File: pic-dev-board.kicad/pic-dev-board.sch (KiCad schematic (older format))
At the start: 44 parts, among them J1 Conn_GP0, J13 Conn_5V_GND, J15 Barrel_Jack_Switch, J16 RUN/~PGM, J17 I2C, J18 GP1(RA1)/RB6, J19 GP2(RA2)/RB4, J2 Conn_GP4, J20 Conn_TRISA, J3 Conn_GP1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

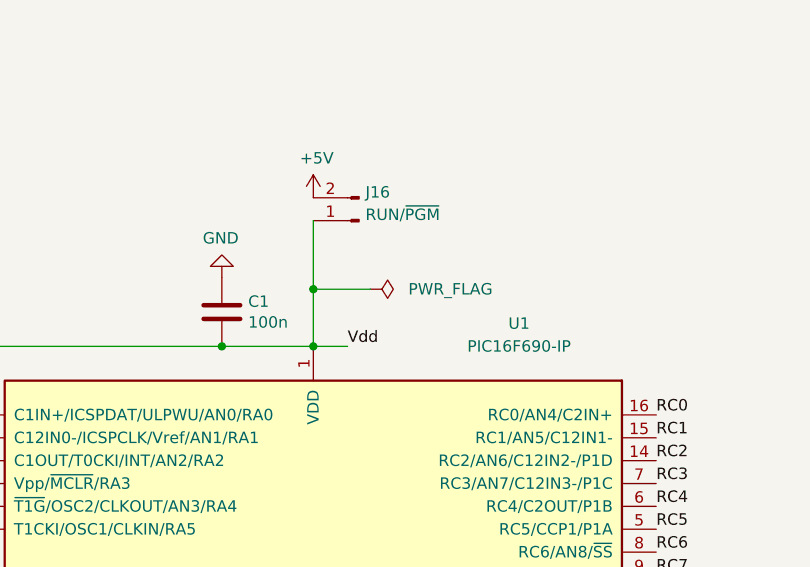
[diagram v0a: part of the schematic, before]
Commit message: removed unnecessary power-flag
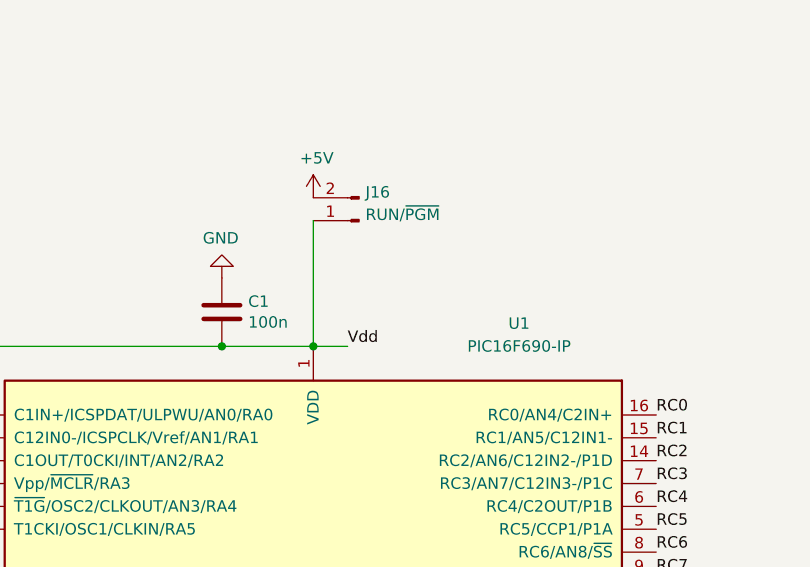
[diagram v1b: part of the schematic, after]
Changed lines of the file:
@@
 Sheet 1 2
 Title "PIC Development Board"
-Date "2020-08-24"
+Date "2020-08-26"
 Rev "2"
 Comp "Bernhard Bablok"
@@
 	-1   0    0    1
 $EndComp
-Wire Wire Line
-	5200 3500 5200 3800
-$Comp
-L power:PWR_FLAG #FLG0104
-U 1 1 5F37108D
-P 5450 3800
-F 0 "#FLG0104" H 5450 3875 50  0001 C CNN
-F 1 "PWR_FLAG" V 5450 4150 50  0000 C CNN
-F 2 "" H 5450 3800 50  0001 C CNN
-F 3 "~" H 5450 3800 50  0001 C CNN
-	1    5450 3800
-	0    1    1    0
-$EndComp
-Connection ~ 5200 3800
-Wire Wire Line
-	5200 3800 5200 4050
-Wire Wire Line
-	5200 3800 5450 3800
 $Comp
 L Connector:Conn_01x04_Male J17
@@
 Wire Wire Line
 	5100 1600 5300 1600
+Wire Wire Line
+	5200 3500 5200 4050
 $EndSCHEMATC

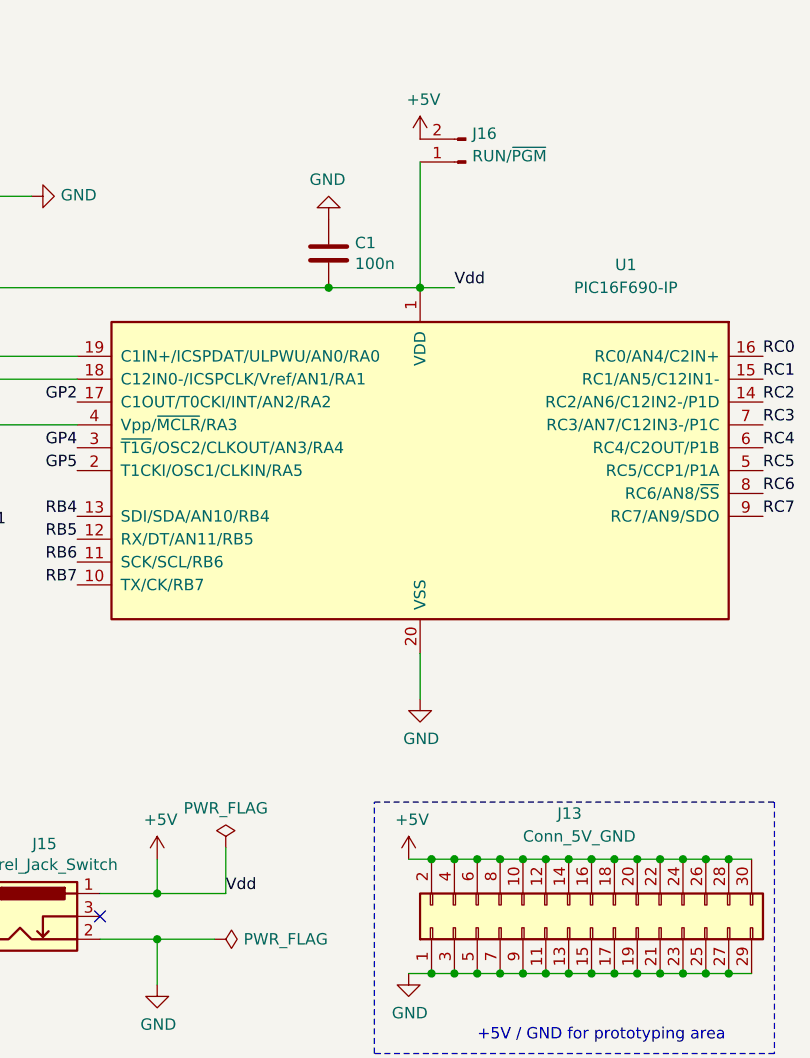
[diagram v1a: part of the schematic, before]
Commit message: reverting Vdd on barrel-jack, power-flag
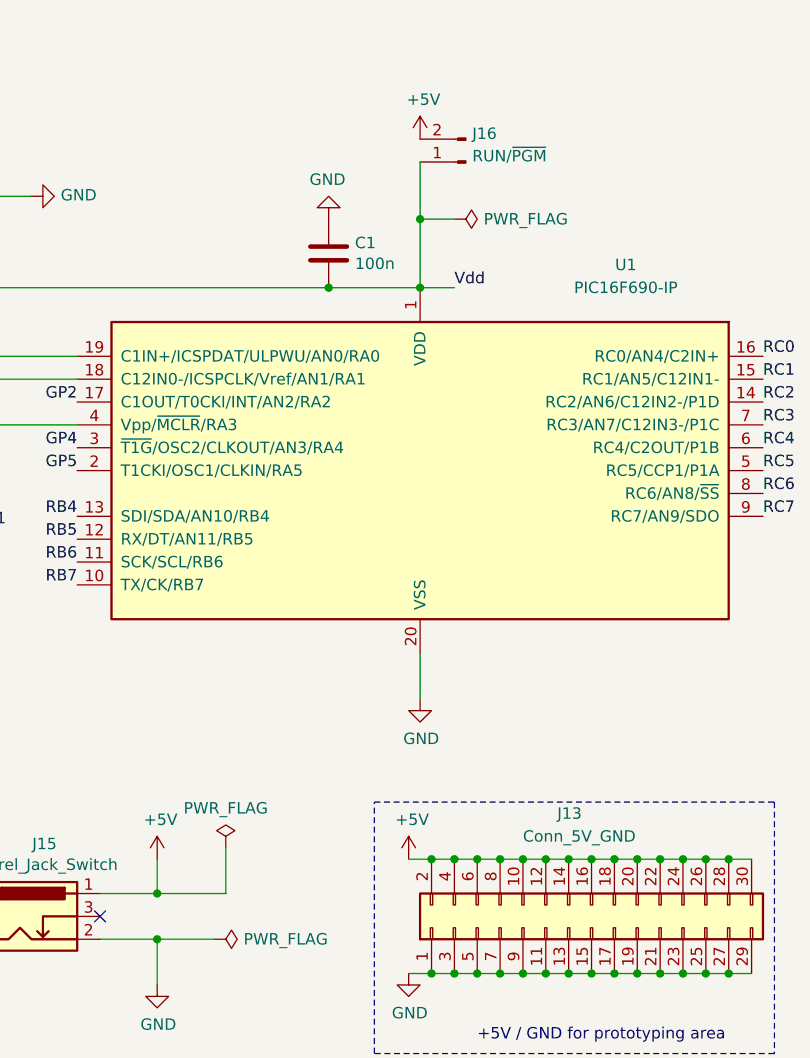
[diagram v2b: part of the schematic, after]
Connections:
- net +5V: no longer C1.2, D6.2 (A), J16.1 (Pin_1), J6.2 (Pin_2), U1.1 (VDD)
- new net Vdd: C1.2, D6.2 (A), J16.1 (Pin_1), J6.2 (Pin_2), U1.1 (VDD)
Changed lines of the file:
@@
 	1800 4650 2100 4650
 NoConn ~ 1800 4350
-$Comp
-L power:+5V #PWR013
-U 1 1 5F36CAAF
-P 5200 3400
-F 0 "#PWR013" H 5200 3250 50  0001 C CNN
-F 1 "+5V" H 5215 3573 50  0000 C CNN
-F 2 "" H 5200 3400 50  0001 C CNN
-F 3 "" H 5200 3400 50  0001 C CNN
-	1    5200 3400
-	1    0    0    -1
-$EndComp
 Text Label 5350 4050 0    50   ~ 0
 Vdd
@@
 Connection ~ 4050 6900
 $Comp
-L Connector:Conn_01x02_Male J16
-U 1 1 5F36E374
-P 5400 3500
-F 0 "J16" H 5372 3376 50  0000 R CNN
-F 1 "RUN/~PGM" H 5372 3474 50  0000 R CNN
-F 2 "Connector_PinHeader_2.54mm:PinHeader_1x02_P2.54mm_Vertical" H 5400 3500 50  0001 C CNN
-F 3 "~" H 5400 3500 50  0001 C CNN
-	1    5400 3500
-	-1   0    0    1
-$EndComp
-$Comp
 L Connector:Conn_01x04_Male J17
 U 1 1 5F37419B
@@
 Wire Notes Line
 	3100 7450 3100 5900
-Text Label 4350 6700 0    50   ~ 0
-Vdd
 Wire Wire Line
 	4350 6500 4350 6700
@@
 	5100 1600 5300 1600
 Wire Wire Line
-	5200 3500 5200 4050
+	5200 3750 5200 4050
+Wire Wire Line
+	5200 3500 5200 3750
+Connection ~ 5200 3750
+Wire Wire Line
+	5350 3750 5200 3750
+$Comp
+L power:PWR_FLAG #FLG0104
+U 1 1 5F47637D
+P 5350 3750
+F 0 "#FLG0104" H 5350 3825 50  0001 C CNN
+F 1 "PWR_FLAG" V 5350 3878 50  0000 L CNN
+F 2 "" H 5350 3750 50  0001 C CNN
+F 3 "~" H 5350 3750 50  0001 C CNN
+	1    5350 3750
+	0    1    1    0
+$EndComp
+$Comp
+L power:+5V #PWR013
+U 1 1 5F36CAAF
+P 5200 3400
+F 0 "#PWR013" H 5200 3250 50  0001 C CNN
+F 1 "+5V" H 5215 3573 50  0000 C CNN
+F 2 "" H 5200 3400 50  0001 C CNN
+F 3 "" H 5200 3400 50  0001 C CNN
+	1    5200 3400
+	1    0    0    -1
+$EndComp
+$Comp
+L Connector:Conn_01x02_Male J16
+U 1 1 5F36E374
+P 5400 3500
+F 0 "J16" H 5372 3376 50  0000 R CNN
+F 1 "RUN/~PGM" H 5372 3474 50  0000 R CNN
+F 2 "Connector_PinHeader_2.54mm:PinHeader_1x02_P2.54mm_Vertical" H 5400 3500 50  0001 C CNN
+F 3 "~" H 5400 3500 50  0001 C CNN
+	1    5400 3500
+	-1   0    0    1
+$EndComp
 $EndSCHEMATC

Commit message: replaced DIP-socket with textool socket
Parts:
- U1: footprint Package_DIP:DIP-20_W7.62mm_Socket -> Socket:DIP_Socket-20_W4.3_W5.08_W7.62_W10.16_W10.9_3M_220-3342-00-0602J
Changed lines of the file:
@@
 Sheet 1 2
 Title "PIC Development Board"
-Date "2020-08-26"
-Rev "2"
+Date "2020-08-29"
+Rev "3"
 Comp "Bernhard Bablok"
 Comment1 "https://github.com/bablokb/pcb-pic-devboard"
@@
 F 0 "U1" H 4300 5750 50  0000 C CNN
 F 1 "PIC16F690-IP" H 4300 5650 50  0000 C CNN
-F 2 "Package_DIP:DIP-20_W7.62mm_Socket" H 5200 4850 50  0001 C CIN
+F 2 "Socket:DIP_Socket-20_W4.3_W5.08_W7.62_W10.16_W10.9_3M_220-3342-00-0602J" H 5200 4850 50  0001 C CIN
 F 3 "http://ww1.microchip.com/downloads/en/DeviceDoc/41262E.pdf" H 5200 4850 50  0001 C CNN
 	1    5200 4850

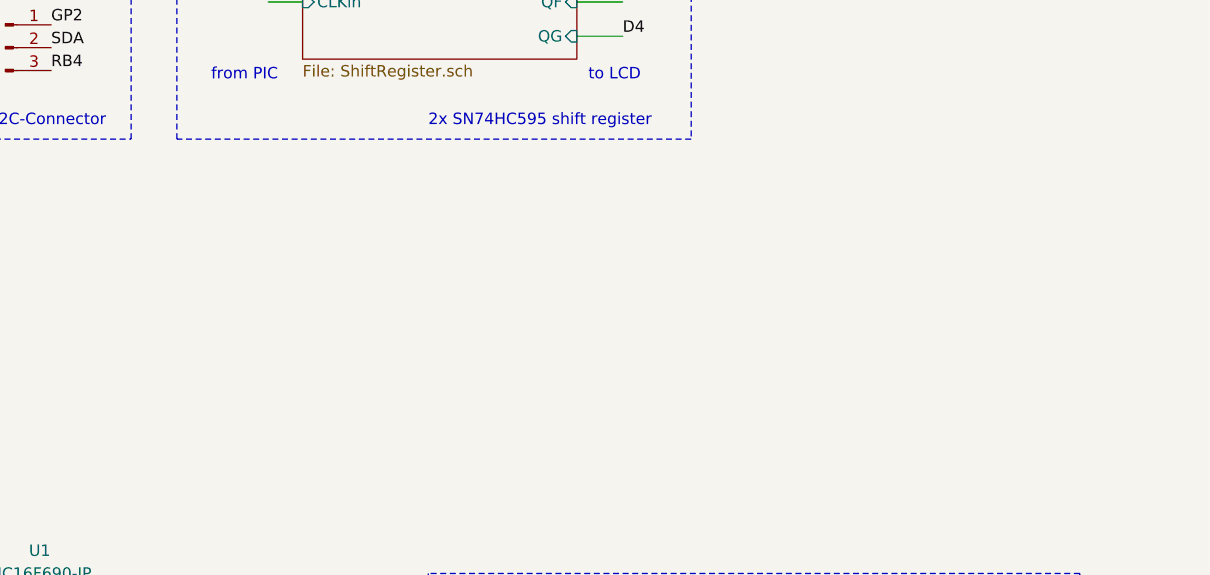
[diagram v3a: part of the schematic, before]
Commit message: Rev4: added SO-8/SOT-223 components to schema to prevent DRC-errors on pcb
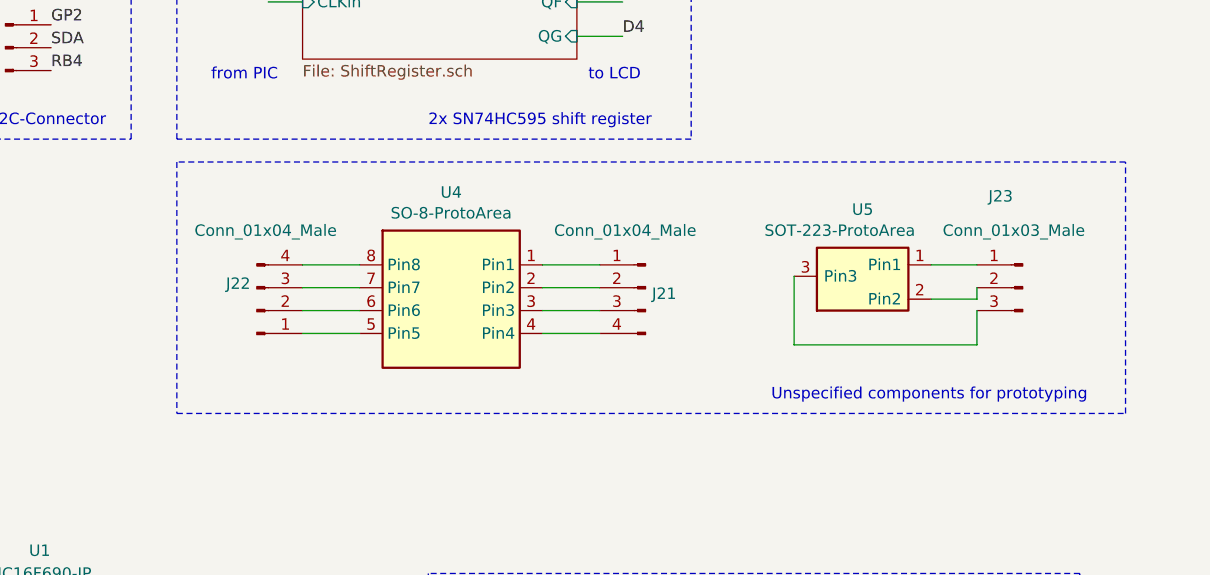
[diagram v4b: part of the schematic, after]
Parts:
- added J21, J22: Conn_01x04_Male, Connector_PinHeader_2.54mm:PinHeader_1x04_P2.54mm_Vertical, symbol Connector:Conn_01x04_Male
- added J23: Conn_01x03_Male, Connector_PinHeader_2.54mm:PinHeader_1x03_P2.54mm_Vertical, symbol Connector:Conn_01x03_Male
- added U4: SO-8-ProtoArea, Package_SO:SO-8_3.9x4.9mm_P1.27mm, symbol Proto_Area:SO-8-ProtoArea
- added U5: SOT-223-ProtoArea, Package_TO_SOT_SMD:SOT-223, symbol Proto_Area:SOT-223-ProtoArea
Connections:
- new net: J21.1 (Pin_1), U4.1 (Pin1)
- new net: J21.2 (Pin_2), U4.2 (Pin2)
- new net: J21.3 (Pin_3), U4.3 (Pin3)
- new net: J21.4 (Pin_4), U4.4 (Pin4)
- new net: J22.1 (Pin_1), U4.5 (Pin5)
- new net: J22.2 (Pin_2), U4.6 (Pin6)
- new net: J22.3 (Pin_3), U4.7 (Pin7)
- new net: J22.4 (Pin_4), U4.8 (Pin8)
- new net: J23.1 (Pin_1), U5.1 (Pin1)
- new net: J23.2 (Pin_2), U5.2 (Pin2)
- new net: J23.3 (Pin_3), U5.3 (Pin3)
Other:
- note added: "Unspecified components for prototyping"
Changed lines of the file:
@@
 Sheet 1 2
 Title "PIC Development Board"
-Date "2020-08-29"
-Rev "3"
+Date "2020-09-07"
+Rev "4"
 Comp "Bernhard Bablok"
 Comment1 "https://github.com/bablokb/pcb-pic-devboard"
@@
 	-1   0    0    1
 $EndComp
+$Comp
+L Proto_Area:SO-8-ProtoArea U4
+U 1 1 5F568960
+P 7900 2850
+F 0 "U4" H 7900 3317 50  0000 C CNN
+F 1 "SO-8-ProtoArea" H 7900 3226 50  0000 C CNN
+F 2 "Package_SO:SO-8_3.9x4.9mm_P1.27mm" H 7950 3400 50  0001 L CNN
+F 3 "https://www.st.com/resource/en/datasheet/stm8s001j3.pdf" H 7800 2950 50  0001 C CNN
+	1    7900 2850
+	1    0    0    -1
+$EndComp
+$Comp
+L Connector:Conn_01x04_Male J22
+U 1 1 5F569B84
+P 7050 2900
+F 0 "J22" H 7022 2782 50  0000 R CNN
+F 1 "Conn_01x04_Male" H 7400 2550 50  0000 R CNN
+F 2 "Connector_PinHeader_2.54mm:PinHeader_1x04_P2.54mm_Vertical" H 7050 2900 50  0001 C CNN
+F 3 "~" H 7050 2900 50  0001 C CNN
+	1    7050 2900
+	1    0    0    1
+$EndComp
+$Comp
+L Connector:Conn_01x04_Male J21
+U 1 1 5F56ABAF
+P 8750 2800
+F 0 "J21" H 8722 2774 50  0000 R CNN
+F 1 "Conn_01x04_Male" H 9150 3050 50  0000 R CNN
+F 2 "Connector_PinHeader_2.54mm:PinHeader_1x04_P2.54mm_Vertical" H 8750 2800 50  0001 C CNN
+F 3 "~" H 8750 2800 50  0001 C CNN
+	1    8750 2800
+	-1   0    0    -1
+$EndComp
+Wire Wire Line
+	8300 2700 8550 2700
+Wire Wire Line
+	8300 2800 8550 2800
+Wire Wire Line
+	8300 2900 8550 2900
+Wire Wire Line
+	8300 3000 8550 3000
+Wire Wire Line
+	7500 2700 7250 2700
+Wire Wire Line
+	7500 2800 7250 2800
+Wire Wire Line
+	7500 2900 7250 2900
+Wire Wire Line
+	7500 3000 7250 3000
+$Comp
+L Proto_Area:SOT-223-ProtoArea U5
+U 1 1 5F5AEBE3
+P 9700 2700
+F 0 "U5" H 9700 2942 50  0000 C CNN
+F 1 "SOT-223-ProtoArea" H 9600 2850 50  0000 C CNN
+F 2 "Package_TO_SOT_SMD:SOT-223" H 9650 3050 50  0001 C CNN
+F 3 "" H 9800 2450 50  0001 C CNN
+	1    9700 2700
+	1    0    0    -1
+$EndComp
+$Comp
+L Connector:Conn_01x03_Male J23
+U 1 1 5F5AFD4C
+P 10400 2800
+F 0 "J23" H 10550 3200 50  0000 R CNN
+F 1 "Conn_01x03_Male" H 10750 3050 50  0000 R CNN
+F 2 "Connector_PinHeader_2.54mm:PinHeader_1x03_P2.54mm_Vertical" H 10400 2800 50  0001 C CNN
+F 3 "~" H 10400 2800 50  0001 C CNN
+	1    10400 2800
+	-1   0    0    -1
+$EndComp
+Wire Wire Line
+	10000 2700 10200 2700
+Wire Wire Line
+	10000 2850 10200 2850
+Wire Wire Line
+	10200 2850 10200 2800
+Wire Wire Line
+	9400 2750 9400 3050
+Wire Wire Line
+	9400 3050 10200 3050
+Wire Wire Line
+	10200 3050 10200 2900
+Wire Notes Line
+	6700 2250 6700 3350
+Wire Notes Line
+	6700 3350 10850 3350
+Wire Notes Line
+	10850 3350 10850 2250
+Wire Notes Line
+	10850 2250 6700 2250
+Text Notes 9300 3300 0    50   ~ 0
+Unspecified components for prototyping
 $EndSCHEMATC
